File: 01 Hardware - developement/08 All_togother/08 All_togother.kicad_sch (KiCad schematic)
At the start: 113 parts, among them IC2 STM32H7A3RIT6TR, J1 POLOLU-2593, J10 Conn_01x03_Pin, J11 Conn_01x03_Pin, J13 ftdi232, J15 ST-link cn3, J16 Boot, J2 ST-link cn6, J3 Conn_01x02_Pin, J4 Conn_01x02_Pin, J5 Conn_01x02_Pin, J6 Conn_01x03_Pin, J7 Conn_01x01_Socket, J8 Conn_01x02_Pin, J9 Conn_01x02_Pin, Q1 BC807, Q2 BC807, SW1 SW_Push_Dual, U1 24C16, U2 LM7805_TO220, X1 8.0MHz 20pF

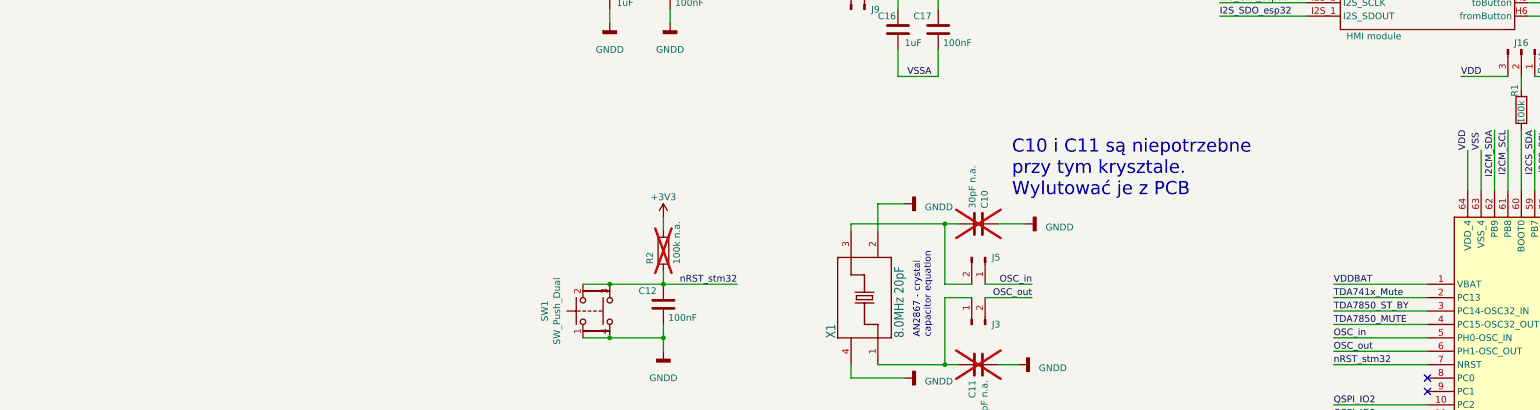
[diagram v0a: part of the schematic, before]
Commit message: dodano uwagi o błędach do schematu.
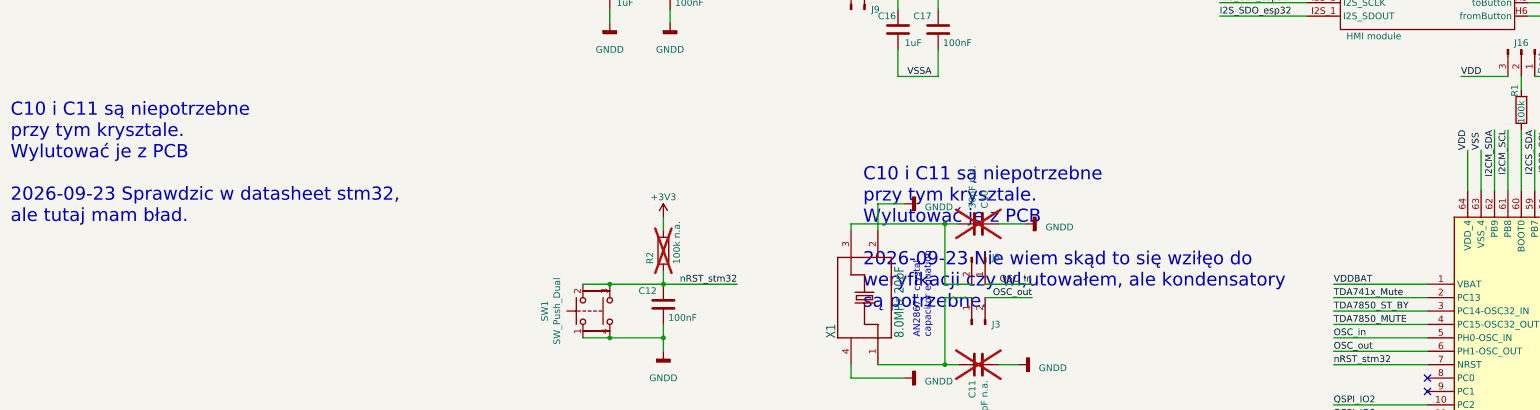
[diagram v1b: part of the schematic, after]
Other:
- note added: "C10 i C11 są niepotrzebne przy tym krysztale. Wylutować je z PCB 2026-09-23 Nie wiem skąd to się wziłęo do weryfikacji czy wl;utowałem, ale kondensatory są potrzebne."
- note added: "C10 i C11 są niepotrzebne przy tym krysztale. Wylutować je z PCB 2026-09-23 Sprawdzic w datasheet stm32, ale tutaj mam bład."
- note removed: "C10 i C11 są niepotrzebne przy tym krysztale. Wylutować je z PCB"
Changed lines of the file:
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@@
 	(generator_version "9.0")
 	(paper "A3")
-	(text "C10 i C11 są niepotrzebne\nprzy tym krysztale.\nWylutować je z PCB"
+	(text "C10 i C11 są niepotrzebne\nprzy tym krysztale.\nWylutować je z PCB\n\n2026-09-23 Nie wiem skąd to się wziłęo do\nweryfikacji czy wl;utowałem, ale kondensatory\nsą potrzebne."
 		(exclude_from_sim no)
-		(at 116.84 113.03 0)
+		(at 88.646 134.366 0)
 		(effects
 			(font
@@
 			)
 			(justify left bottom)
+		)
+	)
+	(text "C10 i C11 są niepotrzebne\nprzy tym krysztale.\nWylutować je z PCB\n\n2026-09-23 Sprawdzic w datasheet stm32,\nale tutaj mam bład."
+		(exclude_from_sim no)
+		(at -72.898 118.11 0)
+		(effects
+			(font
+				(size 2.5 2.5)
+				(color 255 0 34 1)
+			)
+			(justify left bottom)

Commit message: działą interrupt request
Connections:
- net 3V3_det_esp32: now also B7.1 (+3V3), B7.2 (+3V3)
- net Debug_TCK_esp32: now also B7.9 (TCK)
- net Debug_TDI_esp32: now also B7.5 (TDI)
- net Debug_TDO_esp32: now also B7.6 (TDO)
- net Debug_TMS_esp32: now also B7.7 (TMS)
- net nTRST_esp32: now also B7.3 (nRST)
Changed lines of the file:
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@@
 	(wire
 		(pts
-			(xy 152.4 41.91) (xy 172.72 41.91)
+			(xy 152.4 41.91) (xy 176.53 41.91)
 		)
 		(stroke
@@
 	(wire
 		(pts
-			(xy 172.72 39.37) (xy 167.64 39.37)
+			(xy 167.64 39.37) (xy 176.53 39.37)
 		)
 		(stroke
@@
 	(wire
 		(pts
-			(xy 152.4 57.15) (xy 172.72 57.15)
+			(xy 152.4 57.15) (xy 176.53 57.15)
 		)
 		(stroke
@@
 	(wire
 		(pts
-			(xy 167.64 36.83) (xy 172.72 36.83)
+			(xy 167.64 36.83) (xy 176.53 36.83)
 		)
 		(stroke
@@
 	(wire
 		(pts
-			(xy 152.4 49.53) (xy 172.72 49.53)
+			(xy 152.4 49.53) (xy 176.53 49.53)
 		)
 		(stroke
@@
 	(wire
 		(pts
-			(xy 152.4 46.99) (xy 172.72 46.99)
+			(xy 152.4 46.99) (xy 176.53 46.99)
 		)
 		(stroke
@@
 	(wire
 		(pts
-			(xy 152.4 52.07) (xy 172.72 52.07)
+			(xy 152.4 52.07) (xy 176.53 52.07)
 		)
 		(stroke
